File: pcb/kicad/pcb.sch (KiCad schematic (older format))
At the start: 85 parts, among them K0 KEYSW, K0A1 KEYSW, K0B1 KEYSW, K1 KEYSW, K10 KEYSW, K11 KEYSW, K12 KEYSW, K13 KEYSW, K14 KEYSW, K15 KEYSW, K16 KEYSW, K17 KEYSW, K18 KEYSW, K19 KEYSW, K1A1 KEYSW, K1B1 KEYSW, K2 KEYSW, K20 KEYSW, K21 KEYSW, K22 KEYSW, K23 KEYSW, K24 KEYSW, K25 KEYSW, K26 KEYSW, K27 KEYSW, K28 KEYSW, K29 KEYSW, K2A1 KEYSW, K2B1 KEYSW, K3 KEYSW, K33 KEYSW, K34 KEYSW, K35 KEYSW, K36 KEYSW, K37 KEYSW, K38 KEYSW, K4 KEYSW, K5 KEYSW, K6 KEYSW, K7 KEYSW, K8 KEYSW, K9 KEYSW, U1 Elite-C

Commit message: Add support for Choc v1 switches
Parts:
- K0, K0A1, K0B1, K1, K10, K11, K12, K13, K14, K15, K16, K17, K18, K19, K1A1, K1B1, K2, K20, K21, K22, K23, K24, K25, K26, K27, K28, K29, K2A1, K2B1, K3, K33, K34, K35, K36, K37, K38, K4, K5, K6, K7, K8, K9: footprint Keebs:Mx_Alps_100 -> Keebio-Parts:MX-Alps-Choc-1U-NoLED

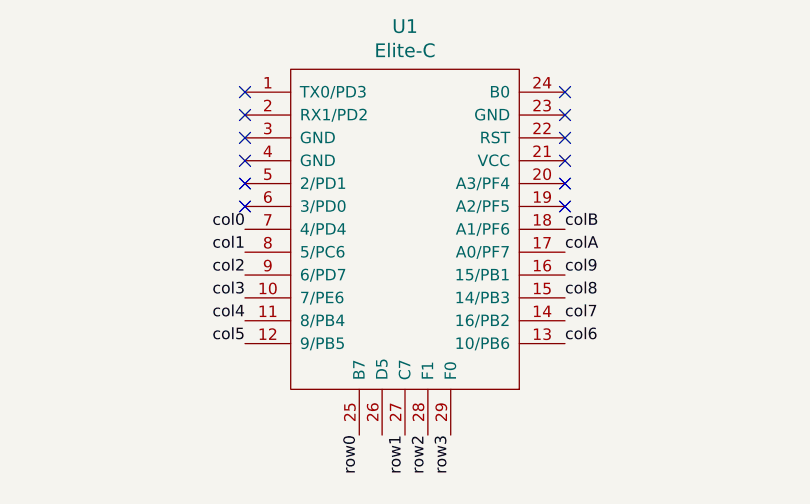
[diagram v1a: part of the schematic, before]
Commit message: Add PCB support for Pro Micro
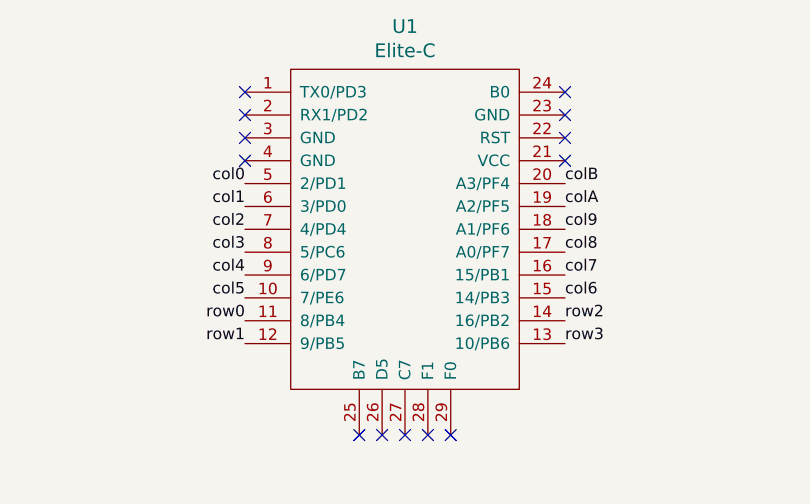
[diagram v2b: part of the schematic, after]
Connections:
- net col0: now also U1.5 (2/PD1); no longer U1.7 (4/PD4)
- net col1: now also U1.6 (3/PD0); no longer U1.8 (5/PC6)
- net col2: now also U1.7 (4/PD4); no longer U1.9 (6/PD7)
- net col3: now also U1.8 (5/PC6); no longer U1.10 (7/PE6)
- net col4: now also U1.9 (6/PD7); no longer U1.11 (8/PB4)
- net col5: now also U1.10 (7/PE6); no longer U1.12 (9/PB5)
- net col6: now also U1.15 (14/PB3); no longer U1.13 (10/PB6)
- net col7: now also U1.16 (15/PB1); no longer U1.14 (16/PB2)
- net col8: now also U1.17 (A0/PF7); no longer U1.15 (14/PB3)
- net col9: now also U1.18 (A1/PF6); no longer U1.16 (15/PB1)
- net colA: now also U1.19 (A2/PF5); no longer U1.17 (A0/PF7)
- net colB: now also U1.20 (A3/PF4); no longer U1.18 (A1/PF6)
- net row0: now also U1.11 (8/PB4); no longer U1.25 (B7)
- net row1: now also U1.12 (9/PB5); no longer U1.27 (C7)
- net row2: now also U1.14 (16/PB2); no longer U1.28 (F1)
- net row3: now also U1.13 (10/PB6); no longer U1.29 (F0)
- no-connect marks 12 -> 13
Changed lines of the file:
@@
 Text Label 12050 1600 0    50   ~ 0
 colB
-Text Label 3425 7175 3    50   ~ 0
+Text Label 4025 6675 0    50   ~ 0
 row2
-Text Label 3525 7175 3    50   ~ 0
+Text Label 4025 6775 0    50   ~ 0
 row3
-Text Label 4025 6775 0    50   ~ 0
+Text Label 4025 6575 0    50   ~ 0
 col6
-Text Label 4025 6675 0    50   ~ 0
+Text Label 4025 6475 0    50   ~ 0
 col7
-Text Label 4025 6575 0    50   ~ 0
+Text Label 4025 6375 0    50   ~ 0
 col8
-Text Label 4025 6475 0    50   ~ 0
+Text Label 4025 6275 0    50   ~ 0
 col9
-Text Label 4025 6375 0    50   ~ 0
+Text Label 4025 6175 0    50   ~ 0
 colA
-Text Label 4025 6275 0    50   ~ 0
+Text Label 4025 6075 0    50   ~ 0
 colB
 Connection ~ 8450 2050
 Wire Wire Line
 	8450 2050 9400 2050
+Text Label 2625 6575 2    50   ~ 0
+col5
+Text Label 2625 6475 2    50   ~ 0
+col4
+Text Label 2625 6375 2    50   ~ 0
+col3
+Text Label 2625 6275 2    50   ~ 0
+col2
+Text Label 2625 6175 2    50   ~ 0
+col1
+Text Label 2625 6075 2    50   ~ 0
+col0
 Text Label 2625 6775 2    50   ~ 0
-col5
+row1
 Text Label 2625 6675 2    50   ~ 0
-col4
-Text Label 2625 6575 2    50   ~ 0
-col3
-Text Label 2625 6475 2    50   ~ 0
-col2
-Text Label 2625 6375 2    50   ~ 0
-col1
-Text Label 2625 6275 2    50   ~ 0
-col0
-Text Label 3325 7175 3    50   ~ 0
-row1
-Text Label 3125 7175 3    50   ~ 0
 row0
-NoConn ~ 2625 6075
+NoConn ~ 3125 7175
 NoConn ~ 4025 5675
 NoConn ~ 4025 5775
 NoConn ~ 4025 5875
 NoConn ~ 4025 5975
-NoConn ~ 4025 6075
-NoConn ~ 4025 6175
-NoConn ~ 2625 6175
+NoConn ~ 3225 7175
+NoConn ~ 3425 7175
+NoConn ~ 3525 7175
 NoConn ~ 2625 5975
 NoConn ~ 2625 5875
@@
 	1    0    0    -1
 $EndComp
+NoConn ~ 3325 7175
 $EndSCHEMATC
